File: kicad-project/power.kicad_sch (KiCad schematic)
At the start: 18 parts

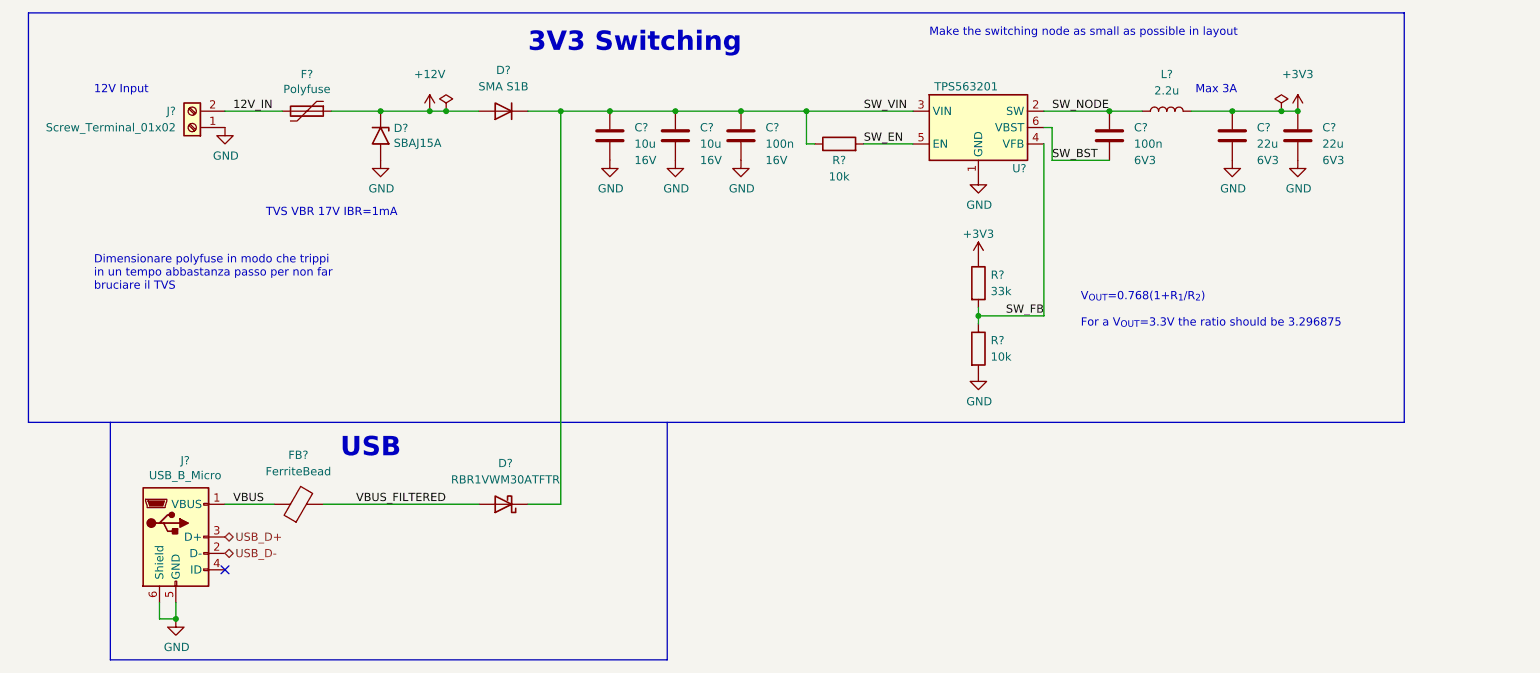
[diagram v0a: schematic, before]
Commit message: hw: add footprints for resistors and capacitors and re-add specs documant that was deleted
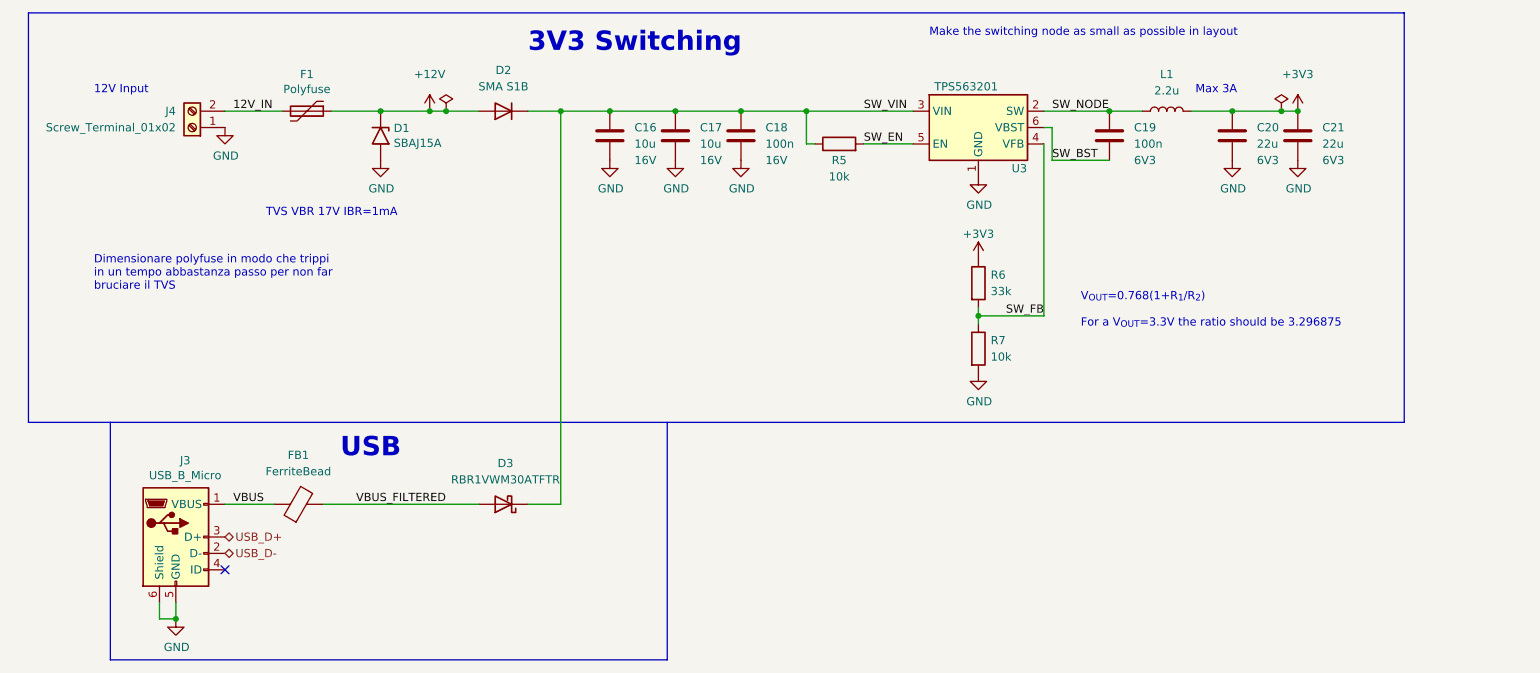
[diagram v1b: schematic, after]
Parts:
- C16, C17, C20, C21: renamed from C?; footprint (none) -> Capacitor_SMD:C_0805_2012Metric
- C18, C19: renamed from C?; footprint (none) -> Capacitor_SMD:C_0603_1608Metric
- D2: renamed from D?; footprint (none) -> Diode_SMD:D_SMA
- J3: renamed from J?; footprint (none) -> Connector_USB:USB_Micro-B_Molex-105133-0001
- J4: renamed from J?; footprint (none) -> TerminalBlock_TE-Connectivity:TerminalBlock_TE_282834-2_1x02_P2.54mm_Horizontal
- R5, R6, R7: renamed from R?; footprint (none) -> Resistor_SMD:R_0603_1608Metric
- gave numbers to parts that had none: 6

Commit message: hw: update root pin and usb connector
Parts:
- J3: value USB_B_Micro -> USB_B_Mini; symbol Connector:USB_B_Micro -> Connector:USB_B_Mini
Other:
- note added: "L1 : Montaggio finale per testare la parte a monte"
- note added: "SMAJ56 (?)"
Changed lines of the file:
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@@
+    (effects (font (size 1.27 1.27)) (justify left bottom))
+  )
+  (text "L1 : Montaggio finale per\n	testare la parte a monte"
+    (at 195.58 52.07 0)
     (effects (font (size 1.27 1.27)) (justify left bottom))
   )
   (text "V_{OUT}=0.768(1+R_{1}/R_{2})\n\nFor a V_{OUT}=3.3V the ratio should be 3.296875"
     (at 178.435 64.135 0)
+    (effects (font (size 1.27 1.27)) (justify left bottom))
+  )
+  (text "SMAJ56 (?)" (at 72.39 39.37 0)
     (effects (font (size 1.27 1.27)) (justify left bottom))
   )
@@
     (pin "6")
   )
-  (symbol (lib_id "Connector:USB_B_Micro") (at 38.1 96.52 0) (unit 1)
+  (symbol (lib_id "Connector:USB_B_Mini") (at 38.1 96.52 0) (unit 1)
     (in_bom yes) (on_board yes)
     (property "Reference" "J3" (id 0) (at 39.5478 84.6582 0))
-    (property "Value" "USB_B_Micro" (id 1) (at 39.5478 86.9696 0))
+    (property "Value" "USB_B_Mini" (id 1) (at 39.5478 86.9696 0))
     (property "Footprint" "Connector_USB:USB_Micro-B_Molex-105133-0001" (id 2) (at 41.91 97.79 0)
       (effects (font (size 1.27 1.27)) hide)

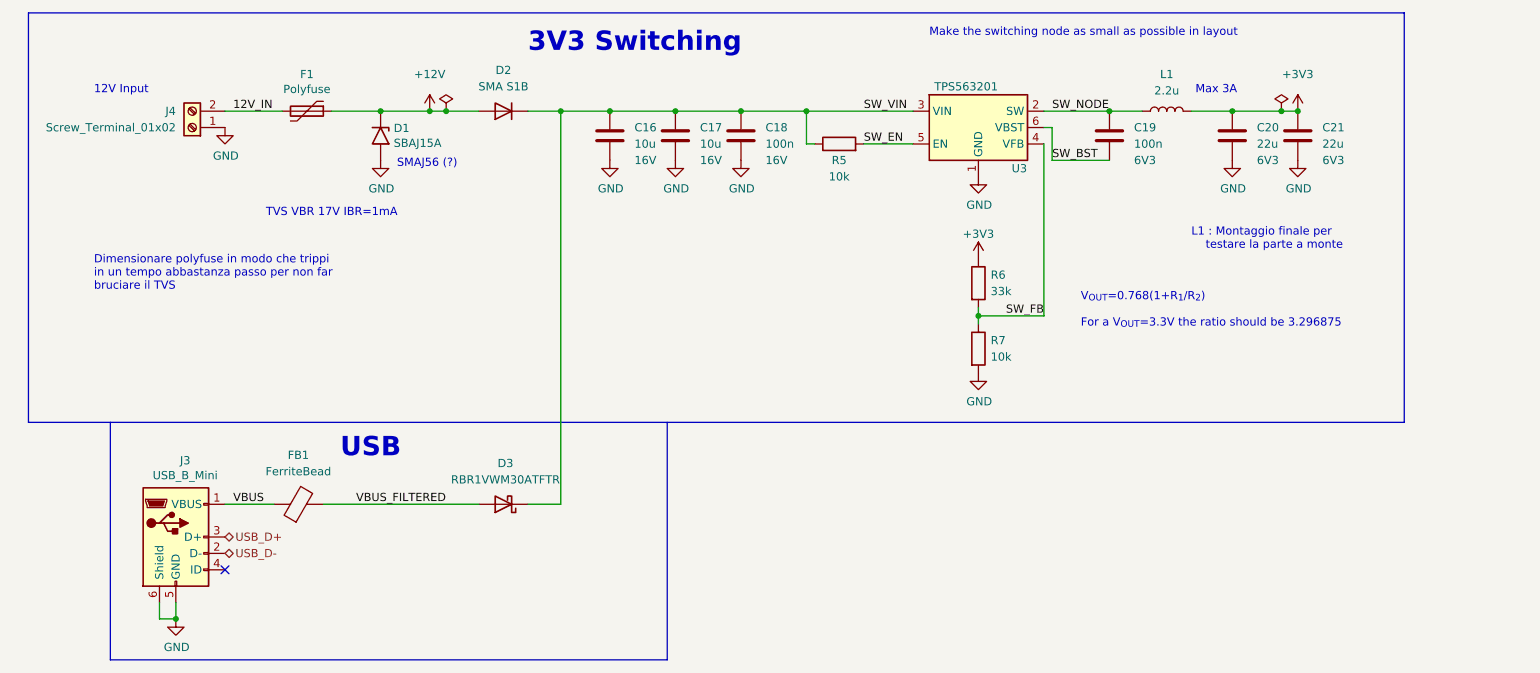
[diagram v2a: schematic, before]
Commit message: hw: part of last checks and footprint assignments
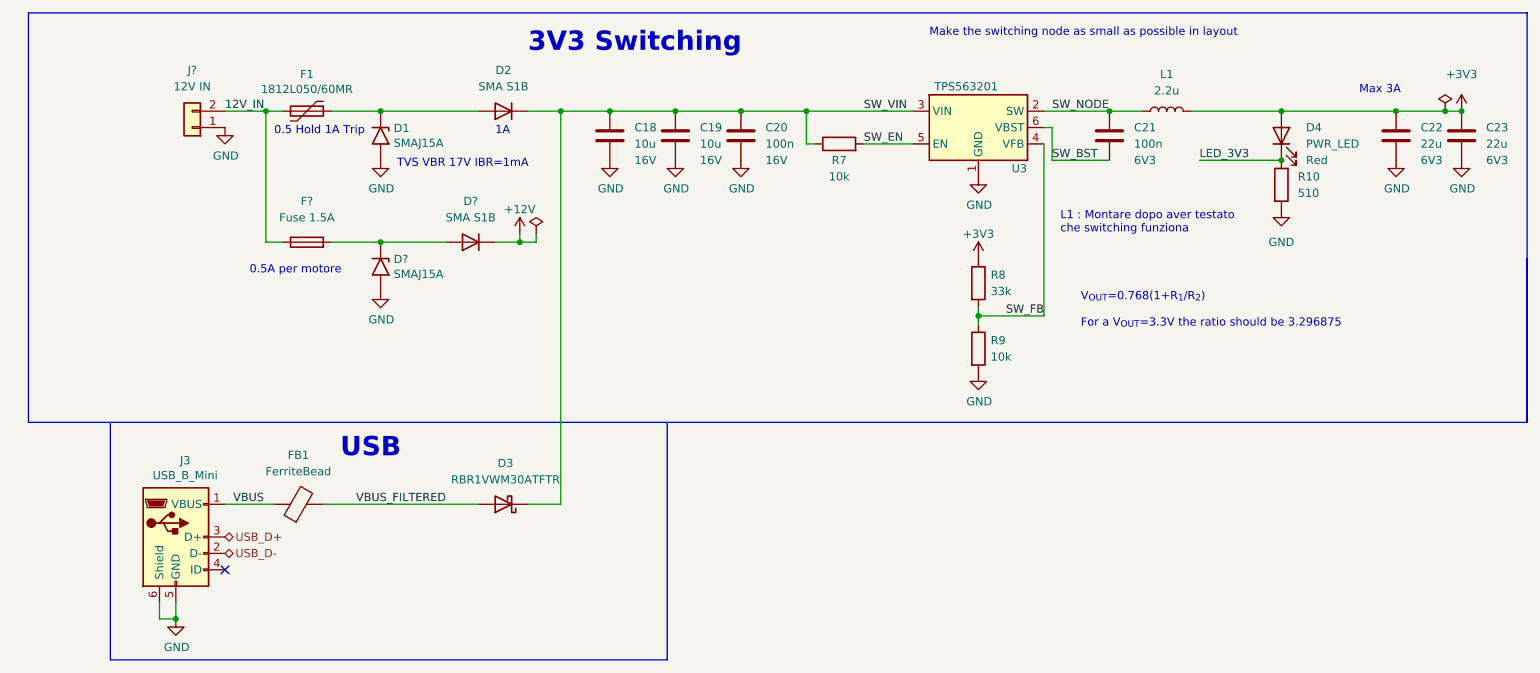
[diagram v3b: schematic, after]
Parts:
- removed J4: Screw_Terminal_01x02, TerminalBlock_TE-Connectivity:TerminalBlock_TE_282834-2_1x02_P2.54mm_Horizontal, symbol Connector:Screw_Terminal_01x02
- added D4: PWR_LED, LED_SMD:LED_0603_1608Metric, symbol Device:LED
- added D?: SMAJ15A, Diode_SMD:D_SMA, symbol Diode:1.5KExxA
- added D?: SMA S1B, Diode_SMD:D_SMA, symbol Diode:1N4007
- added F?: Fuse 1.5A, symbol Device:Fuse
- added J?: 12V IN, Connector_Molex:Molex_Micro-Fit_3.0_43650-0200_1x02_P3.00mm_Horizontal, symbol Connector_Generic:Conn_01x02
- added R10: 510, Resistor_SMD:R_0603_1608Metric, symbol Device:R
- D1: value SBAJ15A -> SMAJ15A; footprint (none) -> Diode_SMD:D_SMA
- F1: value Polyfuse -> 1812L050/60MR
- FB1: footprint (none) -> Inductor_SMD:L_0603_1608Metric
- renumbered C16 to C18, C17 to C19, C18 to C20, C19 to C21, C20 to C22, C21 to C23, R5 to R7, R6 to R8, R7 to R9
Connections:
- net +12V: now also D?.1 (K); no longer D1.1 (A1), D2.2 (A), F1.1
- net +3V3: now also D4.2 (A)
- net 12V_IN: now also F?.1, J?.2 (Pin_2)
- net GND: now also D?.2 (A2), J?.1 (Pin_1), R10.2
- new net: D1.1 (A1), D2.2 (A), F1.1
- new net: D?.1 (A1), D?.2 (A), F?.2
- new net LED_3V3: D4.1 (K), R10.1
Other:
- note added: "0.5 Hold 1A Trip"
- note added: "0.5A per motore"
- note added: "1A"
- note added: "L1 : Montare dopo aver testato che switching funziona"
- note removed: "12V Input"
- note removed: "Dimensionare polyfuse in modo che trippi in un tempo abbastanza passo per non far bruciare il TVS"
- note removed: "L1 : Montaggio finale per testare la parte a monte"
- note removed: "SMAJ56 (?)"
- moved on the sheet: C22, C23

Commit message: commit anonimo di thimas
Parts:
- added TP1, TP2, TP3: TestPoint, TestPoint:TestPoint_Keystone_5005-5009_Compact, symbol Connector:TestPoint
- gave numbers to parts that had none: 4
- renumbered D2 to D4, D3 to D5, D4 to D6
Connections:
- net +12V: now also TP1.1
- net +3V3: now also TP3.1
- net SW_VIN: now also TP2.1
- net LED_3V3 renamed iLED_3V3
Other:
- moved on the sheet: D3

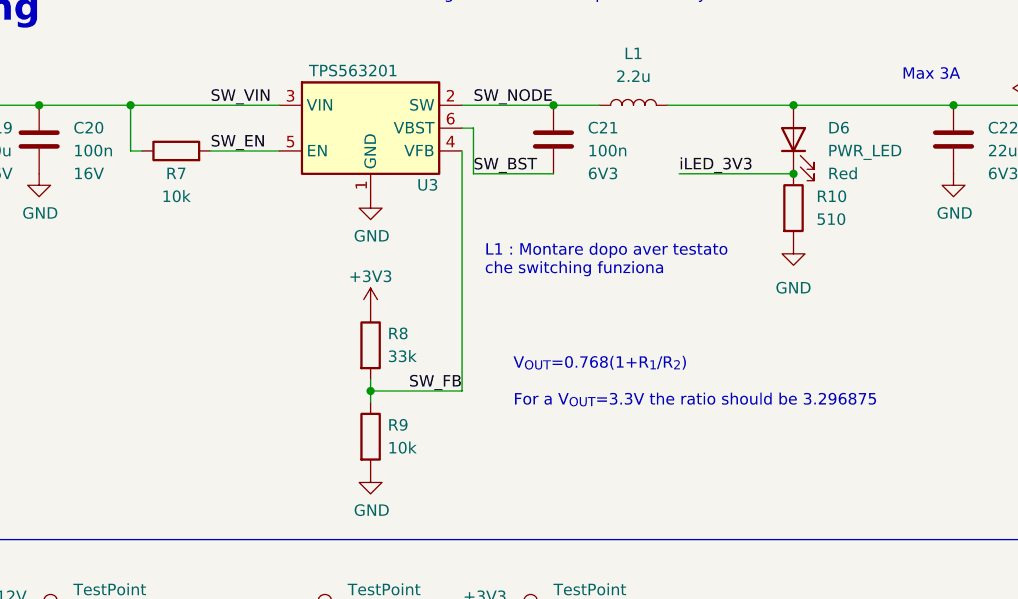
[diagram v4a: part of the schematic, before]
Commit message: hw: add mounting holes
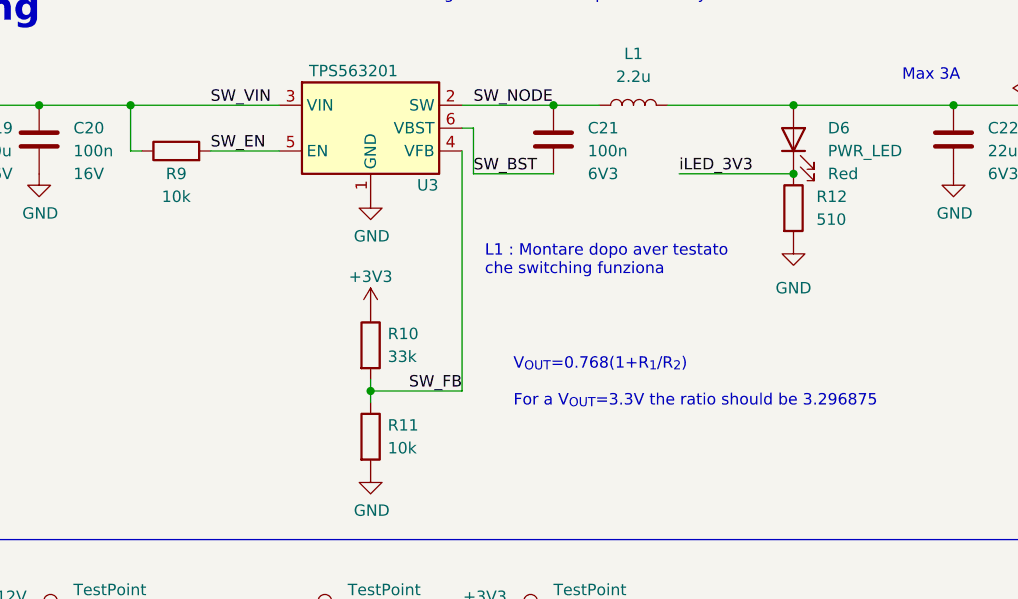
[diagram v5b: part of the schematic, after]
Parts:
- D5: footprint (none) -> Diode_SMD:D_SMA
- renumbered R8 to R10, R9 to R11, R10 to R12, R7 to R9
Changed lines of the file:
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@@
   (symbol (lib_id "Device:R") (at 162.56 57.15 0) (unit 1)
     (in_bom yes) (on_board yes) (fields_autoplaced)
-    (property "Reference" "R8" (id 0) (at 164.465 55.8799 0)
+    (property "Reference" "R10" (id 0) (at 164.465 55.8799 0)
       (effects (font (size 1.27 1.27)) (justify left))
     )
@@
   (symbol (lib_id "Device:R") (at 162.56 67.31 0) (unit 1)
     (in_bom yes) (on_board yes) (fields_autoplaced)
-    (property "Reference" "R9" (id 0) (at 164.465 66.0399 0)
+    (property "Reference" "R11" (id 0) (at 164.465 66.0399 0)
       (effects (font (size 1.27 1.27)) (justify left))
     )
@@
   (symbol (lib_id "Device:R") (at 140.97 35.56 90) (unit 1)
     (in_bom yes) (on_board yes)
-    (property "Reference" "R7" (id 0) (at 140.97 38.1 90))
+    (property "Reference" "R9" (id 0) (at 140.97 38.1 90))
     (property "Value" "10k" (id 1) (at 140.97 40.64 90))
     (property "Footprint" "Resistor_SMD:R_0603_1608Metric" (id 2) (at 140.97 37.338 90)
@@
   (symbol (lib_id "Device:R") (at 209.55 41.91 0) (unit 1)
     (in_bom yes) (on_board yes) (fields_autoplaced)
-    (property "Reference" "R10" (id 0) (at 212.09 40.6399 0)
+    (property "Reference" "R12" (id 0) (at 212.09 40.6399 0)
       (effects (font (size 1.27 1.27)) (justify left))
     )
@@
     (property "Reference" "D5" (id 0) (at 89.2175 85.09 0))
     (property "Value" "RBR1VWM30ATFTR" (id 1) (at 89.2175 87.63 0))
-    (property "Footprint" "" (id 2) (at 88.9 91.44 0)
-      (effects (font (size 1.27 1.27)) hide)
-    )
+    (property "Footprint" "Diode_SMD:D_SMA" (id 2) (at 88.9 91.44 0)
+      (effects (font (size 1.27 1.27)) hide)
+    )

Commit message: hw: add PMDE footprint
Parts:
- D5: footprint Diode_SMD:D_SMA -> ppse_2021:Package-PMDE
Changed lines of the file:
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@@
     (property "Reference" "D5" (id 0) (at 89.2175 85.09 0))
     (property "Value" "RBR1VWM30ATFTR" (id 1) (at 89.2175 87.63 0))
-    (property "Footprint" "Diode_SMD:D_SMA" (id 2) (at 88.9 91.44 0)
+    (property "Footprint" "ppse_2021:Package-PMDE" (id 2) (at 88.9 91.44 0)
       (effects (font (size 1.27 1.27)) hide)
     )
-    (property "Datasheet" "~" (id 3) (at 88.9 91.44 0)
+    (property "Datasheet" "https://docs.rs-online.com/7cac/A700000008315514.pdf" (id 3) (at 88.9 91.44 0)
       (effects (font (size 1.27 1.27)) hide)
     )

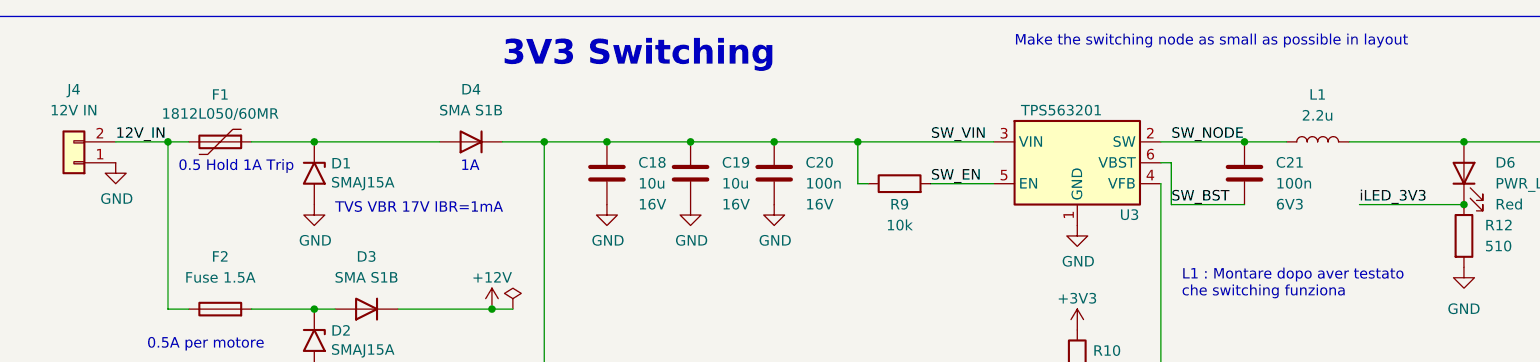
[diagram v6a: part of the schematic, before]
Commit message: hw: add last footprints
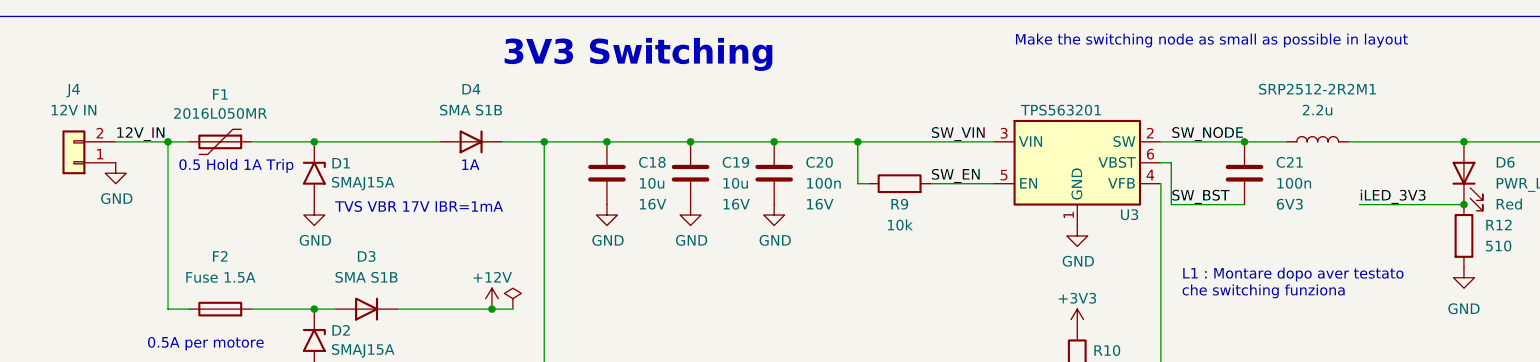
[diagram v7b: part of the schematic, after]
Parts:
- F1: value 1812L050/60MR -> 2016L050MR; footprint (none) -> ppse_2021:2016L Series PPTC
- F2: footprint (none) -> ppse_2021:Fuse Holder
- SRP2512-2R2M1: renamed from L1; footprint (none) -> ppse_2021:Inductor
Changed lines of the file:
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@@
     (in_bom yes) (on_board yes)
     (property "Reference" "F1" (id 0) (at 58.42 24.765 90))
-    (property "Value" "1812L050/60MR" (id 1) (at 58.42 27.0764 90))
-    (property "Footprint" "" (id 2) (at 53.34 31.75 0)
+    (property "Value" "2016L050MR" (id 1) (at 58.42 27.0764 90))
+    (property "Footprint" "ppse_2021:2016L Series PPTC" (id 2) (at 53.34 31.75 0)
       (effects (font (size 1.27 1.27)) (justify left) hide)
     )
-    (property "Datasheet" "~" (id 3) (at 58.42 30.48 0)
+    (property "Datasheet" "https://www.farnell.com/datasheets/664999.pdf" (id 3) (at 58.42 30.48 0)
       (effects (font (size 1.27 1.27)) hide)
     )
@@
   (symbol (lib_id "Device:L") (at 191.77 30.48 90) (unit 1)
     (in_bom yes) (on_board yes) (fields_autoplaced)
-    (property "Reference" "L1" (id 0) (at 191.77 24.765 90))
-    (property "Value" "2.2u" (id 1) (at 191.77 27.305 90))
-    (property "Footprint" "" (id 2) (at 191.77 30.48 0)
-      (effects (font (size 1.27 1.27)) hide)
-    )
-    (property "Datasheet" "~" (id 3) (at 191.77 30.48 0)
+    (property "Reference" "SRP2512-2R2M1" (id 0) (at 191.77 24.13 90))
+    (property "Value" "2.2u" (id 1) (at 191.77 26.67 90))
+    (property "Footprint" "ppse_2021:Inductor" (id 2) (at 191.77 30.48 0)
+      (effects (font (size 1.27 1.27)) hide)
+    )
+    (property "Datasheet" "https://www.mouser.it/datasheet/2/54/SRP2512-1391417.pdf" (id 3) (at 191.77 30.48 0)
       (effects (font (size 1.27 1.27)) hide)
     )
@@
     (property "Reference" "F2" (id 0) (at 58.42 44.45 90))
     (property "Value" "Fuse 1.5A" (id 1) (at 58.42 46.99 90))
-    (property "Footprint" "" (id 2) (at 58.42 52.578 90)
-      (effects (font (size 1.27 1.27)) hide)
-    )
-    (property "Datasheet" "~" (id 3) (at 58.42 50.8 0)
-      (effects (font (size 1.27 1.27)) hide)
-    )
+    (property "Footprint" "ppse_2021:Fuse Holder" (id 2) (at 58.42 52.578 90)
+      (effects (font (size 1.27 1.27)) hide)
+    )
+    (property "Datasheet" "https://www.farnell.com/datasheets/2074958.pdf" (id 3) (at 58.42 50.8 0)
+      (effects (font (size 1.27 1.27)) hide)
+    )

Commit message: hw: first layout draft
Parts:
- J3: footprint Connector_USB:USB_Micro-B_Molex-105133-0001 -> Connector_USB:USB_Mini-B_Wuerth_65100516121_Horizontal
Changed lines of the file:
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@@
     (property "Reference" "J3" (id 0) (at 39.5478 84.6582 0))
     (property "Value" "USB_B_Mini" (id 1) (at 39.5478 86.9696 0))
-    (property "Footprint" "Connector_USB:USB_Micro-B_Molex-105133-0001" (id 2) (at 41.91 97.79 0)
+    (property "Footprint" "Connector_USB:USB_Mini-B_Wuerth_65100516121_Horizontal" (id 2) (at 41.91 97.79 0)
       (effects (font (size 1.27 1.27)) hide)
     )
